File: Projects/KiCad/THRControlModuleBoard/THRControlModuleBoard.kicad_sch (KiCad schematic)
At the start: 24 parts, among them J1 PCC-SMP-K-5, J2 Screw_Terminal_01x02, J5 Conn_02x03_Odd_Even, J6 Conn_02x03_Odd_Even, U1 MAX31856MUD+T

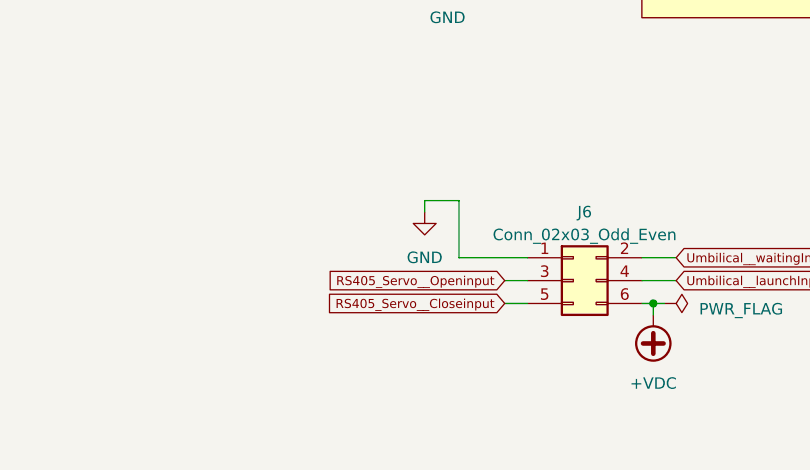
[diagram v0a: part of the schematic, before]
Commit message: 基板形状を決定。部品を配置中
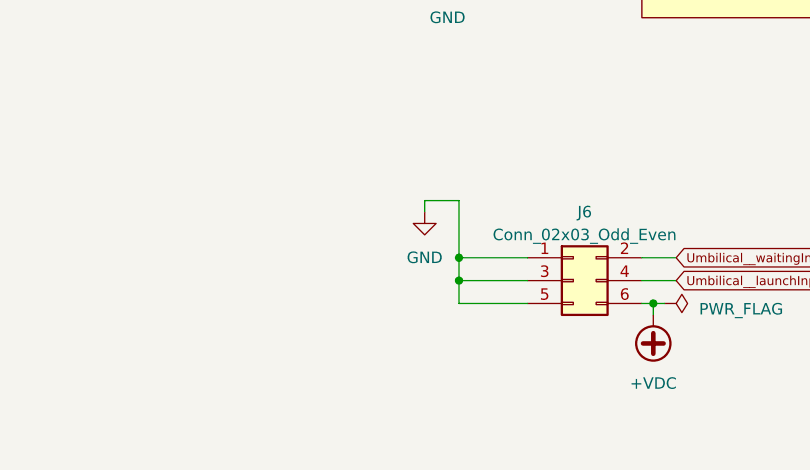
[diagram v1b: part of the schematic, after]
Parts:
- J5, J6: footprint Connector_PinHeader_2.00mm:PinHeader_2x03_P2.00mm_Vertical -> Hirose_Connector:Hirose_DF51A-6DP-2DSA
- U1: footprint MAX31856MUD_T:SOP65P640X110-14N -> SOP65P640X110-14N
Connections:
- net RS405_Servo__Closeinput is gone; now on net GND: J6.5 (Pin_5)
- net RS405_Servo__Openinput is gone; now on net GND: J6.3 (Pin_3)
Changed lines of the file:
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@@
   (junction (at 144.78 111.76) (diameter 0) (color 0 0 0 0)
   )
+  (junction (at 123.19 106.68) (diameter 0) (color 0 0 0 0)
+  )
   (junction (at 187.96 105.41) (diameter 0) (color 0 0 0 0)
   )
@@
   (junction (at 209.55 36.83) (diameter 0) (color 0 0 0 0)
   )
+  (junction (at 123.19 109.22) (diameter 0) (color 0 0 0 0)
+  )
   (junction (at 106.68 62.23) (diameter 0) (color 0 0 0 0)
   )
@@
     (stroke (width 0) (type default))
   )
+  (wire (pts (xy 123.19 109.22) (xy 123.19 106.68))
+    (stroke (width 0) (type default))
+  )
   (wire (pts (xy 110.49 62.23) (xy 106.68 62.23))
     (stroke (width 0) (type default))
@@
     (stroke (width 0) (type default))
   )
+  (wire (pts (xy 130.81 109.22) (xy 123.19 109.22))
+    (stroke (width 0) (type default))
+  )
   (wire (pts (xy 121.92 39.37) (xy 121.92 35.56))
     (stroke (width 0) (type default))
@@
     (stroke (width 0) (type default))
   )
+  (wire (pts (xy 130.81 111.76) (xy 123.19 111.76))
+    (stroke (width 0) (type default))
+  )
   (wire (pts (xy 146.05 111.76) (xy 144.78 111.76))
     (stroke (width 0) (type default))
@@
     (stroke (width 0) (type default))
   )
-  (wire (pts (xy 128.27 109.22) (xy 130.81 109.22))
-    (stroke (width 0) (type default))
-  )
   (wire (pts (xy 209.55 59.69) (xy 226.06 59.69))
     (stroke (width 0) (type default))
@@
     (stroke (width 0) (type default))
   )
+  (wire (pts (xy 123.19 111.76) (xy 123.19 109.22))
+    (stroke (width 0) (type default))
+  )
   (wire (pts (xy 97.79 57.15) (xy 106.68 57.15))
     (stroke (width 0) (type default))
@@
   )
   (wire (pts (xy 204.47 36.83) (xy 204.47 53.34))
-    (stroke (width 0) (type default))
-  )
-  (wire (pts (xy 128.27 111.76) (xy 130.81 111.76))
     (stroke (width 0) (type default))
   )
@@
     )
   )
-  (global_label "RS405_Servo__Openinput" (shape input) (at 128.27 109.22 180) (fields_autoplaced)
-    (effects (font (size 1 1)) (justify right))
-    (property "Intersheetrefs" "${INTERSHEET_REFS}" (at 107.3153 109.22 0)
-      (effects (font (size 1.27 1.27)) (justify right) hide)
-    )
-  )
   (global_label "DRDY" (shape output) (at 184.15 54.61 0) (fields_autoplaced)
     (effects (font (face "KiCad Font") (size 1.27 1.27)) (justify left))
@@
     )
   )
-  (global_label "RS405_Servo__Closeinput" (shape input) (at 128.27 111.76 180) (fields_autoplaced)
-    (effects (font (size 1 1)) (justify right))
-    (property "Intersheetrefs" "${INTERSHEET_REFS}" (at 106.9344 111.76 0)
-      (effects (font (size 1.27 1.27)) (justify right) hide)
-    )
-  )
   (global_label "CAN__H" (shape input) (at 246.38 92.71 180) (fields_autoplaced)
     (effects (font (size 1.27 1.27)) (justify right))
@@
       (effects (font (size 1.27 1.27)))
     )
-    (property "Footprint" "MAX31856MUD_T:SOP65P640X110-14N" (at 156.21 62.23 0)
+    (property "Footprint" "SOP65P640X110-14N" (at 156.21 62.23 0)
       (effects (font (size 1.27 1.27)) (justify bottom) hide)
     )
@@
   (symbol (lib_id "power:GND") (at 182.88 35.56 0) (mirror y) (unit 1)
     (in_bom yes) (on_board yes) (dnp no)
-    (property "Reference" "#PWR010" (at 182.88 41.91 0)
+    (property "Reference" "#PWR09" (at 182.88 41.91 0)
       (effects (font (size 1.27 1.27)) hide)
     )
@@
       (project "THRControlModuleBoard"
         (path "/79fd2516-dad6-414c-bb46-91ee9bfb5006"
-          (reference "#PWR010") (unit 1)
+          (reference "#PWR09") (unit 1)
         )
       )
@@
       (effects (font (size 1.27 1.27)))
     )
-    (property "Footprint" "Connector_PinHeader_2.00mm:PinHeader_2x03_P2.00mm_Vertical" (at 135.89 109.22 0)
+    (property "Footprint" "Hirose_Connector:Hirose_DF51A-6DP-2DSA" (at 135.89 109.22 0)
       (effects (font (size 1.27 1.27)) hide)
     )
@@
       (effects (font (size 1.27 1.27)) (justify right))
     )
-    (property "Footprint" "Connector_PinHeader_2.00mm:PinHeader_2x03_P2.00mm_Vertical" (at 196.85 107.95 0)
+    (property "Footprint" "Hirose_Connector:Hirose_DF51A-6DP-2DSA" (at 196.85 107.95 0)
       (effects (font (size 1.27 1.27)) hide)
     )
@@
   (symbol (lib_id "power:GND") (at 184.15 102.87 0) (unit 1)
     (in_bom yes) (on_board yes) (dnp no) (fields_autoplaced)
-    (property "Reference" "#PWR09" (at 184.15 109.22 0)
+    (property "Reference" "#PWR010" (at 184.15 109.22 0)
       (effects (font (size 1.27 1.27)) hide)
     )
@@
       (project "THRControlModuleBoard"
         (path "/79fd2516-dad6-414c-bb46-91ee9bfb5006"
-          (reference "#PWR09") (unit 1)
+          (reference "#PWR010") (unit 1)
         )
       )
@@
   (symbol (lib_id "power:GND") (at 119.38 101.6 0) (unit 1)
     (in_bom yes) (on_board yes) (dnp no) (fields_autoplaced)
-    (property "Reference" "#PWR04" (at 119.38 107.95 0)
+    (property "Reference" "#PWR03" (at 119.38 107.95 0)
       (effects (font (size 1.27 1.27)) hide)
     )
@@
       (project "THRControlModuleBoard"
         (path "/79fd2516-dad6-414c-bb46-91ee9bfb5006"
-          (reference "#PWR04") (unit 1)
+          (reference "#PWR03") (unit 1)
         )
       )
@@
   (symbol (lib_id "power:GND") (at 121.92 74.93 0) (unit 1)
     (in_bom yes) (on_board yes) (dnp no) (fields_autoplaced)
-    (property "Reference" "#PWR03" (at 121.92 81.28 0)
+    (property "Reference" "#PWR04" (at 121.92 81.28 0)
       (effects (font (size 1.27 1.27)) hide)
     )
@@
       (project "THRControlModuleBoard"
         (path "/79fd2516-dad6-414c-bb46-91ee9bfb5006"
-          (reference "#PWR03") (unit 1)
-        )
-      )
+          (reference "#PWR04") (unit 1)
+        )
+      )

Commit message: 攻めた設計になってるけど動いてくれ…
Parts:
- removed J1: PCC-SMP-K-5, PCC-SMP-K-5:OMEGA_PCC-SMP-K-5, symbol PCC-SMP-K-5:PCC-SMP-K-5
- added D6: LED, symbol Device:LED
- added R24: R, symbol Device:R
- U1: footprint SOP65P640X110-14N -> Package_SO:TSSOP-14_4.4x5mm_P0.65mm
- renumbered J2 to J1
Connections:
- net +12V: now also R24.1
- net GND: now also D6.1 (K)
- new net: D6.2 (A), R24.2
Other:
- moved on the sheet: J1, R1, R2

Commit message: ボード図を更新
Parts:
- D6: footprint (none) -> LED_SMD:LED_0603_1608Metric_Pad1.05x0.95mm_HandSolder
- R24: value R -> 1k; footprint (none) -> Resistor_SMD:R_0603_1608Metric_Pad0.98x0.95mm_HandSolder
- R3, R4, R5: footprint Resistor_SMD:R_0805_2012Metric_Pad1.20x1.40mm_HandSolder -> Resistor_SMD:R_0603_1608Metric_Pad0.98x0.95mm_HandSolder
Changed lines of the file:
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@@
     (stroke (width 0) (type default))
   )
-  (wire (pts (xy 199.39 91.44) (xy 199.39 93.98))
+  (wire (pts (xy 199.39 87.63) (xy 199.39 93.98))
     (stroke (width 0) (type default))
   )
@@
     )
   )
-  (symbol (lib_id "power:+12V") (at 199.39 91.44 0) (unit 1)
-    (in_bom yes) (on_board yes) (dnp no) (fields_autoplaced)
-    (property "Reference" "#PWR040" (at 199.39 95.25 0)
-      (effects (font (size 1.27 1.27)) hide)
-    )
-    (property "Value" "+12V" (at 199.39 87.63 0)
-      (effects (font (size 1.27 1.27)))
-    )
-    (property "Footprint" "" (at 199.39 91.44 0)
-      (effects (font (size 1.27 1.27)) hide)
-    )
-    (property "Datasheet" "" (at 199.39 91.44 0)
+  (symbol (lib_id "power:+12V") (at 199.39 87.63 0) (unit 1)
+    (in_bom yes) (on_board yes) (dnp no) (fields_autoplaced)
+    (property "Reference" "#PWR040" (at 199.39 91.44 0)
+      (effects (font (size 1.27 1.27)) hide)
+    )
+    (property "Value" "+12V" (at 199.39 83.82 0)
+      (effects (font (size 1.27 1.27)))
+    )
+    (property "Footprint" "" (at 199.39 87.63 0)
+      (effects (font (size 1.27 1.27)) hide)
+    )
+    (property "Datasheet" "" (at 199.39 87.63 0)
       (effects (font (size 1.27 1.27)) hide)
     )
@@
       (effects (font (size 1.27 1.27)))
     )
-    (property "Footprint" "" (at 213.36 93.98 0)
+    (property "Footprint" "LED_SMD:LED_0603_1608Metric_Pad1.05x0.95mm_HandSolder" (at 213.36 93.98 0)
       (effects (font (size 1.27 1.27)) hide)
     )
@@
       (effects (font (size 1.27 1.27)) (justify left))
     )
-    (property "Footprint" "Resistor_SMD:R_0805_2012Metric_Pad1.20x1.40mm_HandSolder" (at 207.772 49.53 90)
+    (property "Footprint" "Resistor_SMD:R_0603_1608Metric_Pad0.98x0.95mm_HandSolder" (at 207.772 49.53 90)
       (effects (font (size 1.27 1.27)) hide)
     )
@@
       (effects (font (size 1.27 1.27)) (justify left))
     )
-    (property "Footprint" "Resistor_SMD:R_0805_2012Metric_Pad1.20x1.40mm_HandSolder" (at 202.692 57.15 90)
+    (property "Footprint" "Resistor_SMD:R_0603_1608Metric_Pad0.98x0.95mm_HandSolder" (at 202.692 57.15 90)
       (effects (font (size 1.27 1.27)) hide)
     )
@@
       (effects (font (size 1.27 1.27)))
     )
-    (property "Value" "R" (at 204.47 91.44 90)
-      (effects (font (size 1.27 1.27)))
-    )
-    (property "Footprint" "" (at 204.47 95.758 90)
+    (property "Value" "1k" (at 204.47 91.44 90)
+      (effects (font (size 1.27 1.27)))
+    )
+    (property "Footprint" "Resistor_SMD:R_0603_1608Metric_Pad0.98x0.95mm_HandSolder" (at 204.47 95.758 90)
       (effects (font (size 1.27 1.27)) hide)
     )
@@
       (effects (font (size 1.27 1.27)) (justify left))
     )
-    (property "Footprint" "Resistor_SMD:R_0805_2012Metric_Pad1.20x1.40mm_HandSolder" (at 212.852 41.91 90)
-      (effects (font (size 1.27 1.27)) hide)
-    )
+    (property "Footprint" "Resistor_SMD:R_0603_1608Metric_Pad0.98x0.95mm_HandSolder" (at 212.852 41.91 90)
+      (effects (font (size 1.27 1.27)) hide)
+    )

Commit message: 長時間の動作を確認した。
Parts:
- added D7: 1N4148W, Diode_SMD:D_SOD-123, symbol Diode:1N4148W
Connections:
- net +12V: now also D7.1 (K); no longer J5.2 (Pin_2), R24.1
- new net: D7.2 (A), J5.2 (Pin_2), R24.1
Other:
- moved on the sheet: D6, R24
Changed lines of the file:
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@@
   (junction (at 209.55 59.69) (diameter 0) (color 0 0 0 0)
   )
-  (junction (at 199.39 93.98) (diameter 0) (color 0 0 0 0)
-  )
   (junction (at 214.63 52.07) (diameter 0) (color 0 0 0 0)
   )
@@
   (junction (at 144.78 111.76) (diameter 0) (color 0 0 0 0)
   )
+  (junction (at 199.39 95.25) (diameter 0) (color 0 0 0 0)
+  )
   (junction (at 123.19 106.68) (diameter 0) (color 0 0 0 0)
   )
@@
   (junction (at 184.15 101.6) (diameter 0) (color 0 0 0 0)
   )
-  (wire (pts (xy 210.82 104.14) (xy 210.82 107.95))
+  (wire (pts (xy 210.82 106.68) (xy 210.82 107.95))
     (stroke (width 0) (type default))
   )
@@
     (stroke (width 0) (type default))
   )
-  (wire (pts (xy 217.17 93.98) (xy 218.44 93.98))
+  (wire (pts (xy 218.44 95.25) (xy 218.44 96.52))
+    (stroke (width 0) (type default))
+  )
+  (wire (pts (xy 199.39 88.9) (xy 199.39 95.25))
     (stroke (width 0) (type default))
   )
@@
     (stroke (width 0) (type default))
   )
-  (wire (pts (xy 200.66 93.98) (xy 199.39 93.98))
-    (stroke (width 0) (type default))
-  )
   (wire (pts (xy 204.47 67.31) (xy 215.9 67.31))
     (stroke (width 0) (type default))
@@
     (stroke (width 0) (type default))
   )
-  (wire (pts (xy 199.39 87.63) (xy 199.39 93.98))
-    (stroke (width 0) (type default))
-  )
   (wire (pts (xy 199.39 101.6) (xy 207.01 101.6))
     (stroke (width 0) (type default))
@@
     (stroke (width 0) (type default))
   )
+  (wire (pts (xy 199.39 78.74) (xy 199.39 81.28))
+    (stroke (width 0) (type default))
+  )
   (wire (pts (xy 146.05 111.76) (xy 144.78 111.76))
     (stroke (width 0) (type default))
@@
     (stroke (width 0) (type default))
   )
-  (wire (pts (xy 218.44 93.98) (xy 218.44 95.25))
-    (stroke (width 0) (type default))
-  )
   (wire (pts (xy 175.26 27.94) (xy 175.26 34.29))
     (stroke (width 0) (type default))
@@
     (stroke (width 0) (type default))
   )
+  (wire (pts (xy 199.39 95.25) (xy 200.66 95.25))
+    (stroke (width 0) (type default))
+  )
   (wire (pts (xy 246.38 105.41) (xy 252.73 105.41))
     (stroke (width 0) (type default))
   )
+  (wire (pts (xy 218.44 95.25) (xy 217.17 95.25))
+    (stroke (width 0) (type default))
+  )
   (wire (pts (xy 97.79 54.61) (xy 106.68 54.61))
     (stroke (width 0) (type default))
   )
-  (wire (pts (xy 199.39 93.98) (xy 199.39 101.6))
-    (stroke (width 0) (type default))
-  )
   (wire (pts (xy 187.96 107.95) (xy 187.96 105.41))
     (stroke (width 0) (type default))
@@
     (stroke (width 0) (type default))
   )
+  (wire (pts (xy 199.39 95.25) (xy 199.39 101.6))
+    (stroke (width 0) (type default))
+  )
   (wire (pts (xy 175.26 34.29) (xy 175.26 46.99))
     (stroke (width 0) (type default))
@@
     (stroke (width 0) (type default))
   )
-  (wire (pts (xy 208.28 93.98) (xy 209.55 93.98))
+  (wire (pts (xy 208.28 95.25) (xy 209.55 95.25))
     (stroke (width 0) (type default))
   )
@@
     )
   )
-  (symbol (lib_id "power:+12V") (at 199.39 87.63 0) (unit 1)
-    (in_bom yes) (on_board yes) (dnp no) (fields_autoplaced)
-    (property "Reference" "#PWR040" (at 199.39 91.44 0)
-      (effects (font (size 1.27 1.27)) hide)
-    )
-    (property "Value" "+12V" (at 199.39 83.82 0)
-      (effects (font (size 1.27 1.27)))
-    )
-    (property "Footprint" "" (at 199.39 87.63 0)
-      (effects (font (size 1.27 1.27)) hide)
-    )
-    (property "Datasheet" "" (at 199.39 87.63 0)
+  (symbol (lib_id "power:+12V") (at 199.39 78.74 0) (unit 1)
+    (in_bom yes) (on_board yes) (dnp no) (fields_autoplaced)
+    (property "Reference" "#PWR040" (at 199.39 82.55 0)
+      (effects (font (size 1.27 1.27)) hide)
+    )
+    (property "Value" "+12V" (at 199.39 74.93 0)
+      (effects (font (size 1.27 1.27)))
+    )
+    (property "Footprint" "" (at 199.39 78.74 0)
+      (effects (font (size 1.27 1.27)) hide)
+    )
+    (property "Datasheet" "" (at 199.39 78.74 0)
       (effects (font (size 1.27 1.27)) hide)
     )
@@
     )
   )
-  (symbol (lib_id "Device:LED") (at 213.36 93.98 180) (unit 1)
-    (in_bom yes) (on_board yes) (dnp no) (fields_autoplaced)
-    (property "Reference" "D6" (at 214.9475 87.63 0)
-      (effects (font (size 1.27 1.27)))
-    )
-    (property "Value" "LED" (at 214.9475 90.17 0)
-      (effects (font (size 1.27 1.27)))
-    )
-    (property "Footprint" "LED_SMD:LED_0603_1608Metric_Pad1.05x0.95mm_HandSolder" (at 213.36 93.98 0)
-      (effects (font (size 1.27 1.27)) hide)
-    )
-    (property "Datasheet" "~" (at 213.36 93.98 0)
+  (symbol (lib_id "Device:LED") (at 213.36 95.25 180) (unit 1)
+    (in_bom yes) (on_board yes) (dnp no) (fields_autoplaced)
+    (property "Reference" "D6" (at 214.9475 88.9 0)
+      (effects (font (size 1.27 1.27)))
+    )
+    (property "Value" "LED" (at 214.9475 91.44 0)
+      (effects (font (size 1.27 1.27)))
+    )
+    (property "Footprint" "LED_SMD:LED_0603_1608Metric_Pad1.05x0.95mm_HandSolder" (at 213.36 95.25 0)
+      (effects (font (size 1.27 1.27)) hide)
+    )
+    (property "Datasheet" "~" (at 213.36 95.25 0)
       (effects (font (size 1.27 1.27)) hide)
     )
@@
     )
   )
-  (symbol (lib_id "power:+VDC") (at 210.82 104.14 0) (unit 1)
-    (in_bom yes) (on_board yes) (dnp no) (fields_autoplaced)
-    (property "Reference" "#PWR013" (at 210.82 106.68 0)
-      (effects (font (size 1.27 1.27)) hide)
-    )
-    (property "Value" "+VDC" (at 210.82 97.79 0)
-      (effects (font (size 1.27 1.27)))
-    )
-    (property "Footprint" "" (at 210.82 104.14 0)
-      (effects (font (size 1.27 1.27)) hide)
-    )
-    (property "Datasheet" "" (at 210.82 104.14 0)
+  (symbol (lib_id "power:+VDC") (at 210.82 106.68 0) (unit 1)
+    (in_bom yes) (on_board yes) (dnp no) (fields_autoplaced)
+    (property "Reference" "#PWR013" (at 210.82 109.22 0)
+      (effects (font (size 1.27 1.27)) hide)
+    )
+    (property "Value" "+VDC" (at 210.82 100.33 0)
+      (effects (font (size 1.27 1.27)))
+    )
+    (property "Footprint" "" (at 210.82 106.68 0)
+      (effects (font (size 1.27 1.27)) hide)
+    )
+    (property "Datasheet" "" (at 210.82 106.68 0)
       (effects (font (size 1.27 1.27)) hide)
     )
@@
     )
   )
-  (symbol (lib_id "power:GND") (at 218.44 95.25 0) (unit 1)
-    (in_bom yes) (on_board yes) (dnp no) (fields_autoplaced)
-    (property "Reference" "#PWR053" (at 218.44 101.6 0)
-      (effects (font (size 1.27 1.27)) hide)
-    )
-    (property "Value" "GND" (at 218.44 100.33 0)
-      (effects (font (size 1.27 1.27)))
-    )
-    (property "Footprint" "" (at 218.44 95.25 0)
-      (effects (font (size 1.27 1.27)) hide)
-    )
-    (property "Datasheet" "" (at 218.44 95.25 0)
+  (symbol (lib_id "power:GND") (at 218.44 96.52 0) (unit 1)
+    (in_bom yes) (on_board yes) (dnp no) (fields_autoplaced)
+    (property "Reference" "#PWR053" (at 218.44 102.87 0)
+      (effects (font (size 1.27 1.27)) hide)
+    )
+    (property "Value" "GND" (at 218.44 101.6 0)
+      (effects (font (size 1.27 1.27)))
+    )
+    (property "Footprint" "" (at 218.44 96.52 0)
+      (effects (font (size 1.27 1.27)) hide)
+    )
+    (property "Datasheet" "" (at 218.44 96.52 0)
       (effects (font (size 1.27 1.27)) hide)
     )
@@
         (path "/79fd2516-dad6-414c-bb46-91ee9bfb5006"
           (reference "R3") (unit 1)
+        )
+      )
+    )
+  )
+  (symbol (lib_id "Diode:1N4148W") (at 199.39 85.09 270) (unit 1)
+    (in_bom yes) (on_board yes) (dnp no) (fields_autoplaced)
+    (property "Reference" "D7" (at 201.93 84.455 90)
+      (effects (font (size 1.27 1.27)) (justify left))
+    )
+    (property "Value" "1N4148W" (at 201.93 86.995 90)
+      (effects (font (size 1.27 1.27)) (justify left))
+    )
+    (property "Footprint" "Diode_SMD:D_SOD-123" (at 194.945 85.09 0)
+      (effects (font (size 1.27 1.27)) hide)
+    )
+    (property "Datasheet" "https://www.vishay.com/docs/85748/1n4148w.pdf" (at 199.39 85.09 0)
+      (effects (font (size 1.27 1.27)) hide)
+    )
+    (property "Sim.Device" "D" (at 199.39 85.09 0)
+      (effects (font (size 1.27 1.27)) hide)
+    )
+    (property "Sim.Pins" "1=K 2=A" (at 199.39 85.09 0)
+      (effects (font (size 1.27 1.27)) hide)
+    )
+    (pin "1")
+    (pin "2")
+    (instances
+      (project "THRControlModuleBoard"
+        (path "/79fd2516-dad6-414c-bb46-91ee9bfb5006"
+          (reference "D7") (unit 1)
         )
       )
@@
     )
   )
-  (symbol (lib_id "Device:R") (at 204.47 93.98 90) (unit 1)
-    (in_bom yes) (on_board yes) (dnp no) (fields_autoplaced)
-    (property "Reference" "R24" (at 204.47 88.9 90)
-      (effects (font (size 1.27 1.27)))
-    )
-    (property "Value" "1k" (at 204.47 91.44 90)
-      (effects (font (size 1.27 1.27)))
-    )
-    (property "Footprint" "Resistor_SMD:R_0603_1608Metric_Pad0.98x0.95mm_HandSolder" (at 204.47 95.758 90)
-      (effects (font (size 1.27 1.27)) hide)
-    )
-    (property "Datasheet" "~" (at 204.47 93.98 0)
-      (effects (font (size 1.27 1.27)) hide)
-    )
+  (symbol (lib_id "Device:R") (at 204.47 95.25 90) (unit 1)
+    (in_bom yes) (on_board yes) (dnp no) (fields_autoplaced)
+    (property "Reference" "R24" (at 204.47 90.17 90)
+      (effects (font (size 1.27 1.27)))
+    )
+    (property "Value" "1k" (at 204.47 92.71 90)
+      (effects (font (size 1.27 1.27)))
+    )
+    (property "Footprint" "Resistor_SMD:R_0603_1608Metric_Pad0.98x0.95mm_HandSolder" (at 204.47 97.028 90)
+      (effects (font (size 1.27 1.27)) hide)
+    )
+    (property "Datasheet" "~" (at 204.47 95.25 0)
+      (effects (font (size 1.27 1.27)) hide)
+    )
